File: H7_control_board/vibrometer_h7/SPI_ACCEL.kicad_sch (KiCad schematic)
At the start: 8 parts, among them J601 Conn_01x08_Socket, J602 Conn_01x08_Socket

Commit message: working on getting ERC to run... almost there!
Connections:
- net SPI_CS: no longer names the net of J602.2 (Pin_2), XL601.12 (CS)
- net SPI_MISO: no longer names the net of J602.5 (Pin_5), XL601.1 (SDO/SA0)
- net SPI_MOSI: no longer names the net of J602.4 (Pin_4), XL601.14 (SDA)
- net SPI_SCLK: no longer names the net of J602.3 (Pin_3), XL601.13 (SCL)
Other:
- note added: "SPI_CS"
- note added: "SPI_INT1"
- note added: "SPI_INT2"
- note added: "SPI_MISO"
- note added: "SPI_MOSI"
- note added: "SPI_SCLK"
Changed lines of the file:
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@@
-	)
-	(junction
-		(at 133.35 92.71)
-		(diameter 0)
-		(color 0 0 0 0)
 	)
 	(junction
@@
 	)
 	(junction
-		(at 133.35 87.63)
-		(diameter 0)
-		(color 0 0 0 0)
-	)
-	(junction
-		(at 133.35 90.17)
-		(diameter 0)
-		(color 0 0 0 0)
-	)
-	(junction
-		(at 133.35 85.09)
-		(diameter 0)
-		(color 0 0 0 0)
-	)
-	(junction
-		(at 133.35 80.01)
-		(diameter 0)
-		(color 0 0 0 0)
-	)
-	(junction
 		(at 165.1 64.77)
 		(diameter 0)
 		(color 0 0 0 0)
 	)
-	(junction
-		(at 133.35 82.55)
-		(diameter 0)
-		(color 0 0 0 0)
-	)
 	(no_connect
 		(at 149.86 82.55)
@@
 	(wire
 		(pts
-			(xy 115.57 87.63) (xy 133.35 87.63)
-		)
-		(stroke
-			(width 0)
-			(type default)
-		)
-	)
-	(wire
-		(pts
 			(xy 149.86 77.47) (xy 144.78 77.47)
 		)
@@
 	(wire
 		(pts
-			(xy 115.57 82.55) (xy 133.35 82.55)
-		)
-		(stroke
-			(width 0)
-			(type default)
-		)
-	)
-	(wire
-		(pts
-			(xy 115.57 92.71) (xy 133.35 92.71)
-		)
-		(stroke
-			(width 0)
-			(type default)
-		)
-	)
-	(wire
-		(pts
-			(xy 115.57 85.09) (xy 133.35 85.09)
-		)
-		(stroke
-			(width 0)
-			(type default)
-		)
-	)
-	(wire
-		(pts
 			(xy 133.35 90.17) (xy 149.86 90.17)
 		)
@@
 	(wire
 		(pts
-			(xy 115.57 80.01) (xy 133.35 80.01)
-		)
-		(stroke
-			(width 0)
-			(type default)
-		)
-	)
-	(wire
-		(pts
 			(xy 133.35 80.01) (xy 140.97 80.01)
 		)
@@
 		(pts
 			(xy 205.74 76.2) (xy 226.06 76.2)
-		)
-		(stroke
-			(width 0)
-			(type default)
-		)
-	)
-	(wire
-		(pts
-			(xy 115.57 90.17) (xy 133.35 90.17)
 		)
 		(stroke
@@
 		)
 	)
-	(label "SPI_INT1"
-		(at 115.57 80.01 0)
-		(fields_autoplaced yes)
-		(effects
-			(font
-				(size 1.27 1.27)
-			)
-			(justify left bottom)
+	(text "SPI_SCLK"
+		(exclude_from_sim no)
+		(at 126.746 91.186 0)
+		(effects
+			(font
+				(size 1.27 1.27)
+			)
+			(justify right bottom)
+		)
+	)
+	(text "SPI_INT2"
+		(exclude_from_sim no)
+		(at 126.746 83.566 0)
+		(effects
+			(font
+				(size 1.27 1.27)
+			)
+			(justify right bottom)
+		)
+	)
+	(text "SPI_MOSI"
+		(exclude_from_sim no)
+		(at 126.746 88.646 0)
+		(effects
+			(font
+				(size 1.27 1.27)
+			)
+			(justify right bottom)
+		)
+	)
+	(text "SPI_MISO"
+		(exclude_from_sim no)
+		(at 126.746 86.106 0)
+		(effects
+			(font
+				(size 1.27 1.27)
+			)
+			(justify right bottom)
+		)
+	)
+	(text "SPI_CS"
+		(exclude_from_sim no)
+		(at 126.746 93.726 0)
+		(effects
+			(font
+				(size 1.27 1.27)
+			)
+			(justify right bottom)
+		)
+	)
+	(text "SPI_INT1"
+		(exclude_from_sim no)
+		(at 126.746 81.026 0)
+		(effects
+			(font
+				(size 1.27 1.27)
+			)
+			(justify right bottom)
 		)
 	)
@@
 		)
 	)
-	(label "SPI_INT2"
-		(at 115.57 82.55 0)
-		(fields_autoplaced yes)
-		(effects
-			(font
-				(size 1.27 1.27)
-			)
-			(justify left bottom)
-		)
-	)
 	(label "INT1"
 		(at 140.97 80.01 180)
@@
 		)
 	)
-	(label "SPI_CS"
-		(at 115.57 92.71 0)
-		(fields_autoplaced yes)
-		(effects
-			(font
-				(size 1.27 1.27)
-			)
-			(justify left bottom)
-		)
-	)
 	(label "INT2"
 		(at 140.97 82.55 180)
@@
 		)
 	)
-	(label "SPI_MOSI"
-		(at 115.57 87.63 0)
-		(fields_autoplaced yes)
-		(effects
-			(font
-				(size 1.27 1.27)
-			)
-			(justify left bottom)
-		)
-	)
-	(label "SPI_MISO"
-		(at 115.57 85.09 0)
-		(fields_autoplaced yes)
-		(effects
-			(font
-				(size 1.27 1.27)
-			)
-			(justify left bottom)
-		)
-	)
-	(label "SPI_SCLK"
-		(at 115.57 90.17 0)
-		(fields_autoplaced yes)
-		(effects
-			(font
-				(size 1.27 1.27)
-			)
-			(justify left bottom)
-		)
-	)

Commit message: started part selection
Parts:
- C601, C602: footprint (none) -> Capacitor_SMD:C_0603_1608Metric
- XL601: LCSC (none) -> C967633
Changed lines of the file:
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@@
 			)
 		)
-		(property "Footprint" ""
+		(property "Footprint" "Capacitor_SMD:C_0603_1608Metric"
 			(at 206.7052 72.39 0)
 			(effects
@@
 			)
 		)
-		(property "Footprint" ""
+		(property "Footprint" "Capacitor_SMD:C_0603_1608Metric"
 			(at 195.2752 72.39 0)
 			(effects
@@
 			(at 165.1 85.09 0)
 			(effects
+				(font
+					(size 1.27 1.27)
+				)
+				(hide yes)
+			)
+		)
+		(property "LCSC" "C967633"
+			(at 165.1 85.09 0)
+			(effects

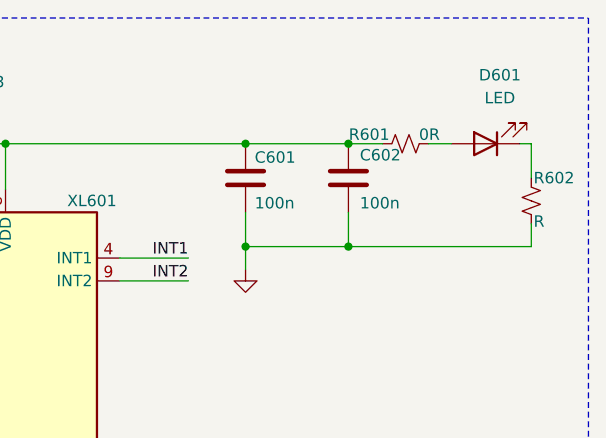
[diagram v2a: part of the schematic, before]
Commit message: component selection, headphone amp circuit specs
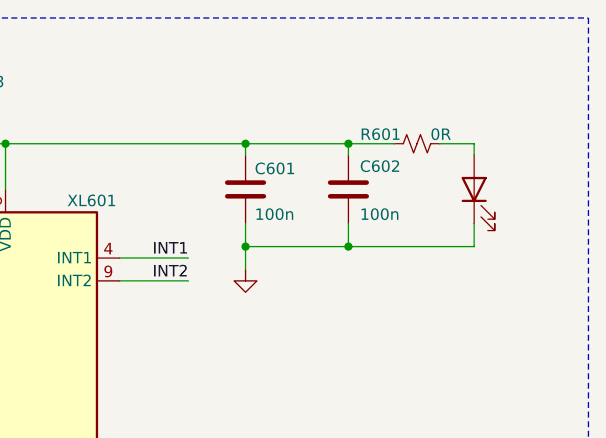
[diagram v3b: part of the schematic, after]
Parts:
- removed R602: R, symbol Device:R_Small_US
- C601, C602: footprint Capacitor_SMD:C_0603_1608Metric -> Capacitor_SMD:C_0402_1005Metric_Pad0.74x0.62mm_HandSolder; LCSC (none) -> C307331
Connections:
- net GND: now also D601.1 (K)
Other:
- moved on the sheet: C601, C602, R601
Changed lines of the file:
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@@
 	(wire
 		(pts
-			(xy 205.74 72.39) (xy 205.74 76.2)
+			(xy 205.74 73.66) (xy 205.74 76.2)
 		)
 		(stroke
@@
 	(wire
 		(pts
-			(xy 226.06 64.77) (xy 226.06 68.58)
-		)
-		(stroke
-			(width 0)
-			(type default)
-		)
-	)
-	(wire
-		(pts
 			(xy 80.01 80.01) (xy 86.36 80.01)
 		)
@@
 	(wire
 		(pts
-			(xy 214.63 64.77) (xy 217.17 64.77)
+			(xy 215.9 64.77) (xy 219.71 64.77)
 		)
 		(stroke
@@
 	(wire
 		(pts
+			(xy 194.31 66.04) (xy 194.31 64.77)
+		)
+		(stroke
+			(width 0)
+			(type default)
+		)
+	)
+	(wire
+		(pts
+			(xy 219.71 73.66) (xy 219.71 76.2)
+		)
+		(stroke
+			(width 0)
+			(type default)
+		)
+	)
+	(wire
+		(pts
 			(xy 133.35 90.17) (xy 149.86 90.17)
 		)
@@
 	(wire
 		(pts
+			(xy 205.74 66.04) (xy 205.74 64.77)
+		)
+		(stroke
+			(width 0)
+			(type default)
+		)
+	)
+	(wire
+		(pts
 			(xy 167.64 64.77) (xy 167.64 69.85)
 		)
@@
 	(wire
 		(pts
-			(xy 194.31 72.39) (xy 194.31 76.2)
+			(xy 194.31 73.66) (xy 194.31 76.2)
 		)
 		(stroke
@@
 	(wire
 		(pts
-			(xy 205.74 76.2) (xy 226.06 76.2)
-		)
-		(stroke
-			(width 0)
-			(type default)
-		)
-	)
-	(wire
-		(pts
-			(xy 226.06 73.66) (xy 226.06 76.2)
-		)
-		(stroke
-			(width 0)
-			(type default)
-		)
-	)
-	(wire
-		(pts
-			(xy 224.79 64.77) (xy 226.06 64.77)
+			(xy 205.74 76.2) (xy 219.71 76.2)
 		)
 		(stroke
@@
 	(wire
 		(pts
-			(xy 205.74 64.77) (xy 209.55 64.77)
+			(xy 205.74 64.77) (xy 210.82 64.77)
 		)
 		(stroke
@@
 		(pts
 			(xy 165.1 64.77) (xy 167.64 64.77)
+		)
+		(stroke
+			(width 0)
+			(type default)
+		)
+	)
+	(wire
+		(pts
+			(xy 219.71 64.77) (xy 219.71 66.04)
 		)
 		(stroke
@@
 	(symbol
 		(lib_id "Device:C")
-		(at 205.74 68.58 0)
+		(at 205.74 69.85 0)
 		(unit 1)
 		(exclude_from_sim no)
@@
 		(dnp no)
 		(property "Reference" "C602"
-			(at 207.01 66.04 0)
+			(at 207.01 67.31 0)
 			(effects
 				(font
@@
 		)
 		(property "Value" "100n"
-			(at 207.01 71.374 0)
+			(at 207.01 72.644 0)
 			(effects
 				(font
@@
 			)
 		)
-		(property "Footprint" "Capacitor_SMD:C_0603_1608Metric"
-			(at 206.7052 72.39 0)
-			(effects
-				(font
-					(size 1.27 1.27)
-				)
-				(hide yes)
-			)
-		)
-		(property "Datasheet" "~"
-			(at 205.74 68.58 0)
+		(property "Footprint" "Capacitor_SMD:C_0402_1005Metric_Pad0.74x0.62mm_HandSolder"
+			(at 206.7052 73.66 0)
+			(effects
+				(font
+					(size 1.27 1.27)
+				)
+				(hide yes)
+			)
+		)
+		(property "Datasheet" "https://wmsc.lcsc.com/wmsc/upload/file/pdf/v2/lcsc/2304140030_Samsung-Electro-Mechanics-CL05B104KB54PNC_C307331.pdf"
+			(at 205.74 69.85 0)
 			(effects
 				(font
@@
 		)
 		(property "Description" "Unpolarized capacitor"
-			(at 205.74 68.58 0)
+			(at 205.74 69.85 0)
+			(effects
+				(font
+					(size 1.27 1.27)
+				)
+				(hide yes)
+			)
+		)
+		(property "LCSC" "C307331"
+			(at 205.74 69.85 0)
 			(effects
 				(font
@@
 	)
 	(symbol
-		(lib_id "Device:R_Small_US")
-		(at 226.06 71.12 0)
-		(unit 1)
-		(exclude_from_sim no)
-		(in_bom yes)
-		(on_board yes)
-		(dnp no)
-		(property "Reference" "R602"
-			(at 226.314 68.58 0)
-			(effects
-				(font
-					(size 1.27 1.27)
-				)
-				(justify left)
-			)
-		)
-		(property "Value" "R"
-			(at 226.314 73.406 0)
-			(effects
-				(font
-					(size 1.27 1.27)
-				)
-				(justify left)
-			)
-		)
-		(property "Footprint" ""
-			(at 226.06 71.12 0)
-			(effects
-				(font
-					(size 1.27 1.27)
-				)
-				(hide yes)
-			)
-		)
-		(property "Datasheet" "~"
-			(at 226.06 71.12 0)
-			(effects
-				(font
-					(size 1.27 1.27)
-				)
-				(hide yes)
-			)
-		)
-		(property "Description" "Resistor, small US symbol"
-			(at 226.06 71.12 0)
-			(effects
-				(font
-					(size 1.27 1.27)
-				)
-				(hide yes)
-			)
-		)
-		(pin "1"
-		)
-		(pin "2"
-		)
-		(instances
-			(project "vibrometer_h7"
-				(path "/18de6987-156a-4b34-871e-cbbe1d261986/719d72ab-d813-461f-9482-52ce573716fd/4d0578b7-7312-4298-97a0-94006dea87de"
-					(reference "R602")
-					(unit 1)
-				)
-				(path "/18de6987-156a-4b34-871e-cbbe1d261986/719d72ab-d813-461f-9482-52ce573716fd/d33e5db2-c968-4012-a875-f240ab3119de"
-					(reference "R802")
-					(unit 1)
-				)
-				(path "/18de6987-156a-4b34-871e-cbbe1d261986/719d72ab-d813-461f-9482-52ce573716fd/e082b3de-4b18-4be4-ba81-d49e87b940c1"
-					(reference "R702")
-					(unit 1)
-				)
-			)
-		)
-	)
-	(symbol
 		(lib_id "Device:C")
-		(at 194.31 68.58 0)
+		(at 194.31 69.85 0)
 		(unit 1)
 		(exclude_from_sim no)
@@
 		(dnp no)
 		(property "Reference" "C601"
-			(at 195.326 66.294 0)
+			(at 195.326 67.564 0)
 			(effects
 				(font
@@
 		)
 		(property "Value" "100n"
-			(at 195.326 71.374 0)
+			(at 195.326 72.644 0)
 			(effects
 				(font
@@
 			)
 		)
-		(property "Footprint" "Capacitor_SMD:C_0603_1608Metric"
-			(at 195.2752 72.39 0)
-			(effects
-				(font
-					(size 1.27 1.27)
-				)
-				(hide yes)
-			)
-		)
-		(property "Datasheet" "~"
-			(at 194.31 68.58 0)
+		(property "Footprint" "Capacitor_SMD:C_0402_1005Metric_Pad0.74x0.62mm_HandSolder"
+			(at 195.2752 73.66 0)
+			(effects
+				(font
+					(size 1.27 1.27)
+				)
+				(hide yes)
+			)
+		)
+		(property "Datasheet" "https://wmsc.lcsc.com/wmsc/upload/file/pdf/v2/lcsc/2304140030_Samsung-Electro-Mechanics-CL05B104KB54PNC_C307331.pdf"
+			(at 194.31 69.85 0)
 			(effects
 				(font
@@
 		)
 		(property "Description" "Unpolarized capacitor"
-			(at 194.31 68.58 0)
+			(at 194.31 69.85 0)
+			(effects
+				(font
+					(size 1.27 1.27)
+				)
+				(hide yes)
+			)
+		)
+		(property "LCSC" "C307331"
+			(at 194.31 69.85 0)
 			(effects
 				(font
@@
 	(symbol
 		(lib_id "Device:R_Small_US")
-		(at 212.09 64.77 90)
+		(at 213.36 64.77 90)
 		(unit 1)
 		(exclude_from_sim no)
@@
 		(dnp no)
 		(property "Reference" "R601"
-			(at 210.312 63.754 90)
+			(at 211.582 63.754 90)
 			(effects
 				(font
@@
 		)
 		(property "Value" "0R"
-			(at 215.9 63.754 90)
+			(at 217.17 63.754 90)
 			(effects
 				(font
@@
 		)
 		(property "Footprint" ""
-			(at 212.09 64.77 0)
+			(at 213.36 64.77 0)
 			(effects
 				(font
@@
 		)
 		(property "Datasheet" "~"
-			(at 212.09 64.77 0)
+			(at 213.36 64.77 0)
 			(effects
 				(font
@@
 		)
 		(property "Description" "Resistor, small US symbol"
-			(at 212.09 64.77 0)
+			(at 213.36 64.77 0)
 			(effects
 				(font
@@
 	(symbol
 		(lib_id "Device:LED")
-		(at 220.98 64.77 180)
+		(at 219.71 69.85 90)
 		(unit 1)
 		(exclude_from_sim no)
@@
 		(fields_autoplaced yes)
 		(property "Reference" "D601"
-			(at 222.5675 57.15 0)
-			(effects
-				(font
-					(size 1.27 1.27)
-				)
+			(at 223.52 70.1674 90)
+			(effects
+				(font
+					(size 1.27 1.27)
+				)
+				(justify right)
+				(hide yes)
 			)
 		)
 		(property "Value" "LED"
-			(at 222.5675 59.69 0)
-			(effects
-				(font
-					(size 1.27 1.27)
-				)
+			(at 223.52 72.7074 90)
+			(effects
+				(font
+					(size 1.27 1.27)
+				)
+				(justify right)
+				(hide yes)
 			)
 		)
 		(property "Footprint" ""
-			(at 220.98 64.77 0)
+			(at 219.71 69.85 0)
 			(effects
 				(font
@@
 		)
 		(property "Datasheet" "~"
-			(at 220.98 64.77 0)
+			(at 219.71 69.85 0)
 			(effects
 				(font
@@
 		)
 		(property "Description" "Light emitting diode"
-			(at 220.98 64.77 0)
-			(effects
-				(font
+			(at 219.71 69.85 0)
+			(effects
+				(font

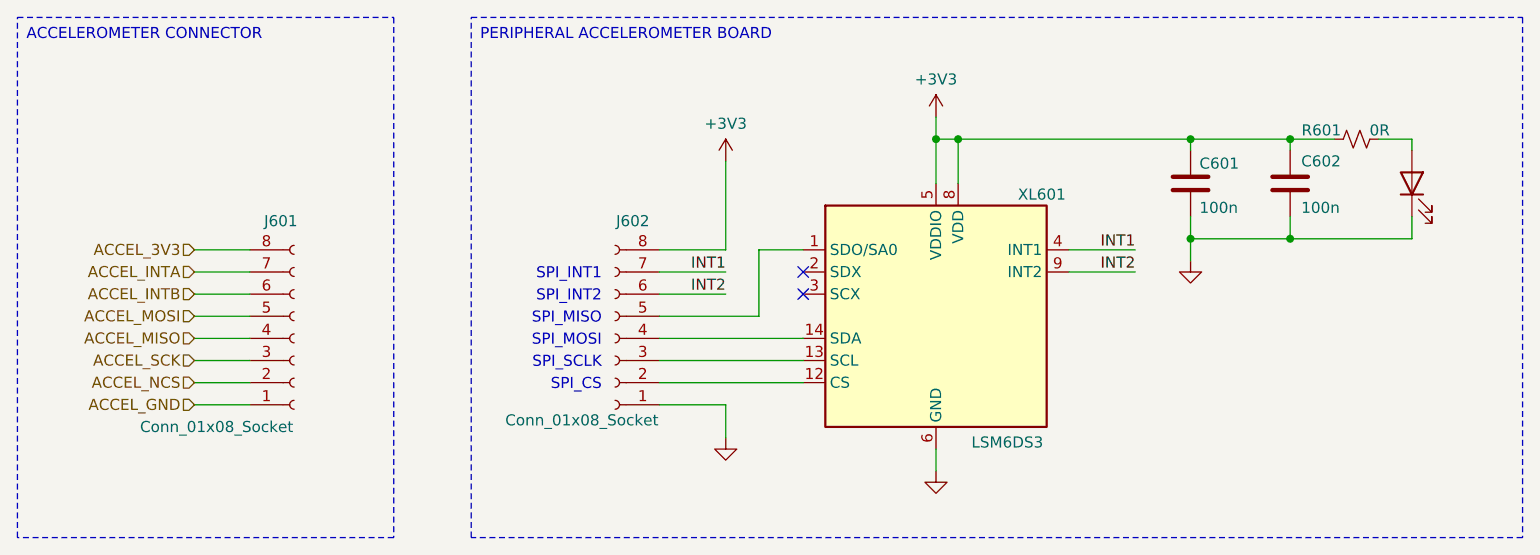
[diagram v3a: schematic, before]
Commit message: part selection for audio, schematic cleanup
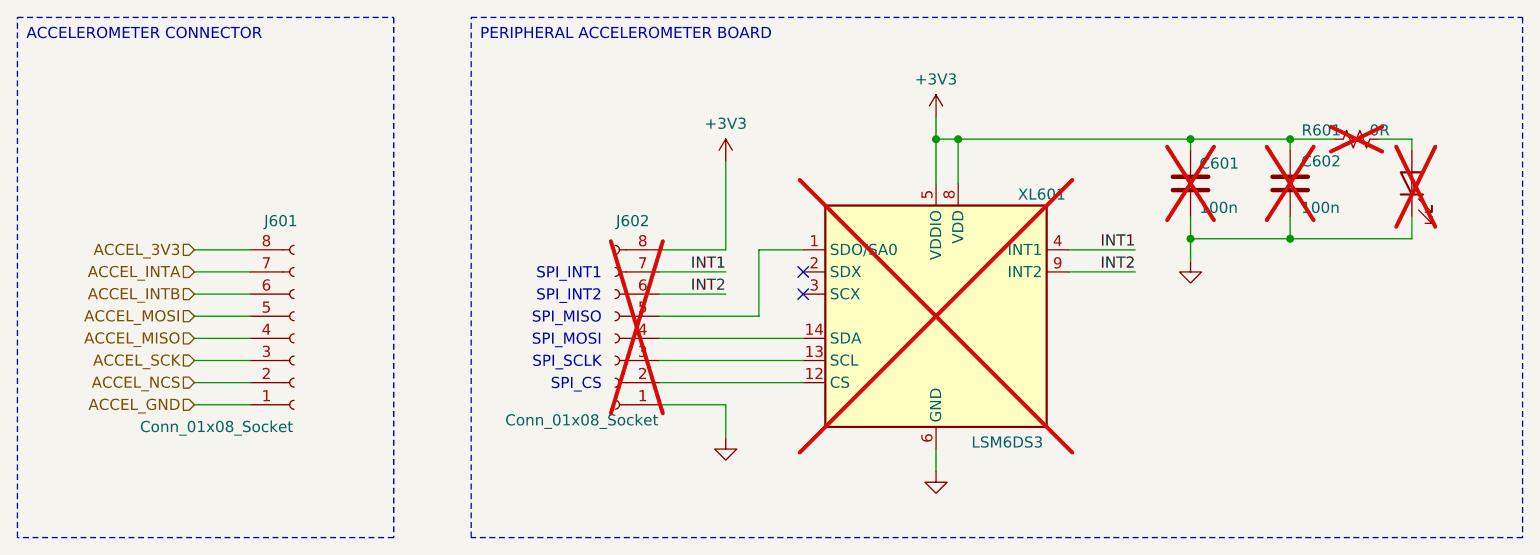
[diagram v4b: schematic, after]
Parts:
- C601, C602, D601, J602, R601, XL601: now not fitted
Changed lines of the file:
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@@
 		(in_bom yes)
 		(on_board yes)
-		(dnp no)
+		(dnp yes)
 		(property "Reference" "C602"
 			(at 207.01 67.31 0)
@@
 		(in_bom yes)
 		(on_board yes)
-		(dnp no)
+		(dnp yes)
 		(property "Reference" "C601"
 			(at 195.326 67.564 0)
@@
 		(in_bom yes)
 		(on_board yes)
-		(dnp no)
+		(dnp yes)
 		(property "Reference" "XL601"
 			(at 174.498 71.12 0)
@@
 		(in_bom yes)
 		(on_board yes)
-		(dnp no)
+		(dnp yes)
 		(property "Reference" "R601"
 			(at 211.582 63.754 90)
@@
 		(in_bom yes)
 		(on_board yes)
-		(dnp no)
+		(dnp yes)
 		(property "Reference" "J602"
 			(at 130.302 74.168 0)
@@
 		(in_bom yes)
 		(on_board yes)
-		(dnp no)
+		(dnp yes)
 		(fields_autoplaced yes)
 		(property "Reference" "D601"

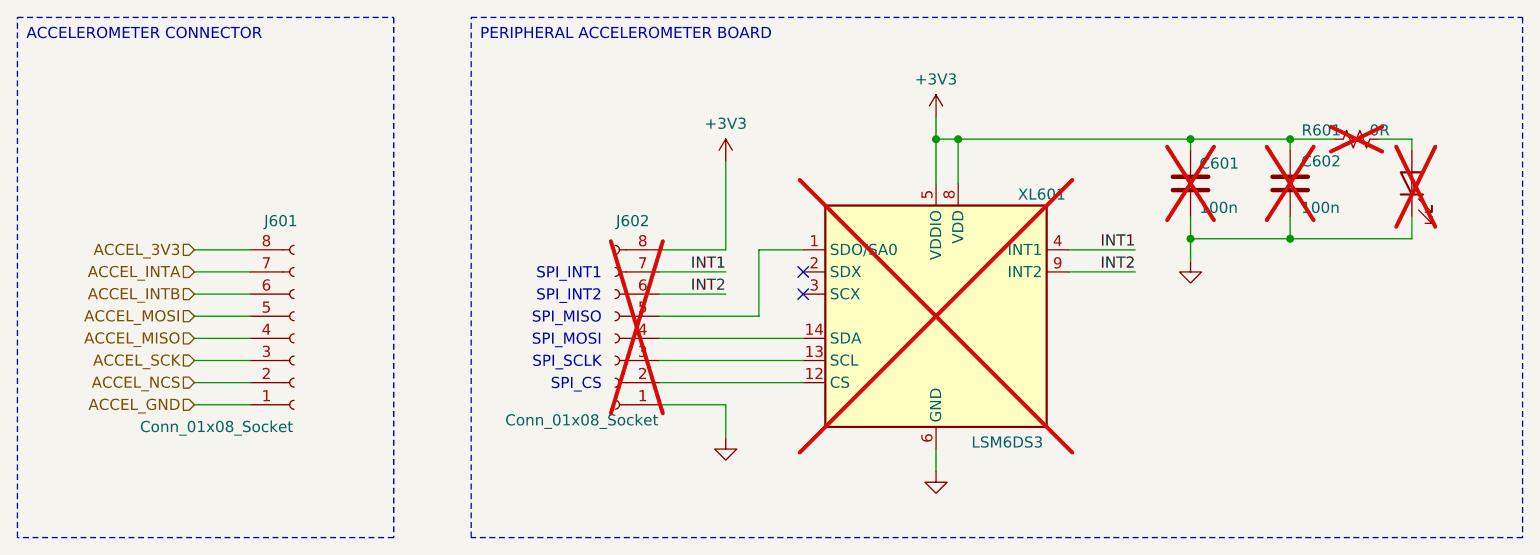
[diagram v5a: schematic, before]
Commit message: selected strobe LEDs, schematic cleanup
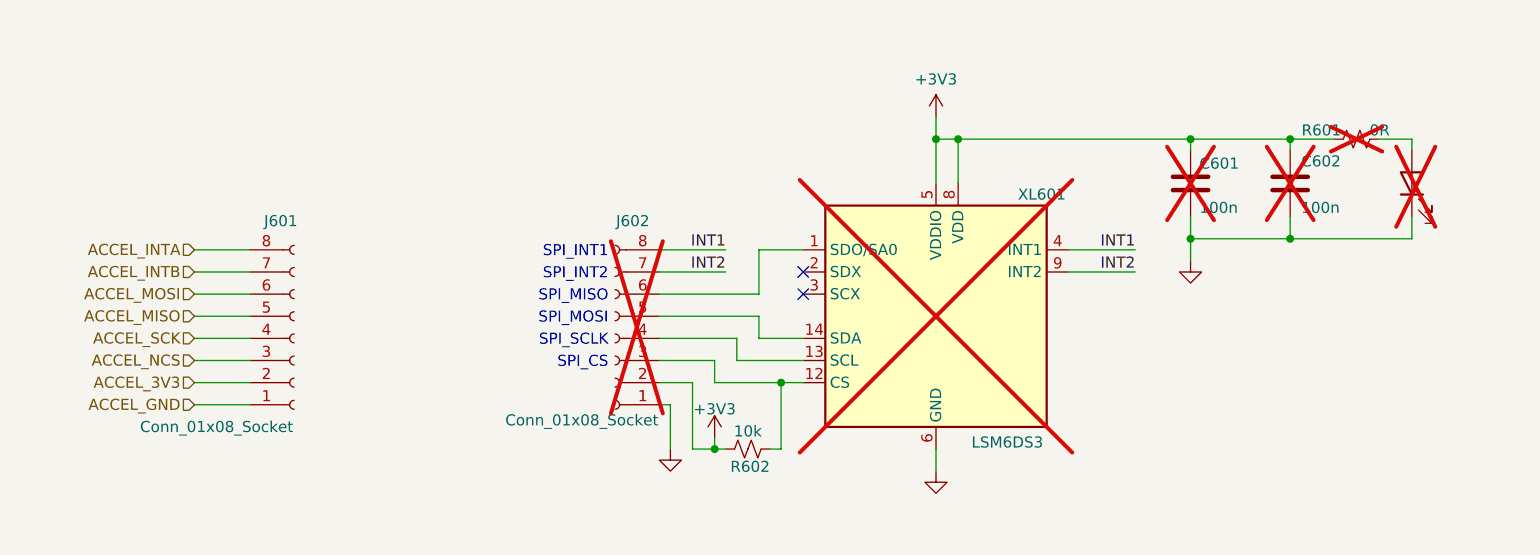
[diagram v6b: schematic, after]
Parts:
- added R602: 10k, symbol Device:R_Small_US
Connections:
- net +3V3: now also J602.2 (Pin_2), R602.2; no longer J602.8 (Pin_8)
- net ACCEL_3V3: now also J601.2 (Pin_2); no longer J601.8 (Pin_8)
- net ACCEL_INTA: now also J601.8 (Pin_8); no longer J601.7 (Pin_7)
- net ACCEL_INTB: now also J601.7 (Pin_7); no longer J601.6 (Pin_6)
- net ACCEL_MISO: now also J601.5 (Pin_5); no longer J601.4 (Pin_4)
- net ACCEL_MOSI: now also J601.6 (Pin_6); no longer J601.5 (Pin_5)
- net ACCEL_NCS: now also J601.3 (Pin_3); no longer J601.2 (Pin_2)
- net ACCEL_SCK: now also J601.4 (Pin_4); no longer J601.3 (Pin_3)
- net INT1: now also J602.8 (Pin_8); no longer J602.7 (Pin_7)
- net INT2: now also J602.7 (Pin_7); no longer J602.6 (Pin_6)
- net at XL601.1 (SDO/SA0): now also J602.6 (Pin_6); no longer J602.5 (Pin_5)
- net at XL601.12 (CS): now also J602.3 (Pin_3), R602.1; no longer J602.2 (Pin_2)
- net at XL601.13 (SCL): now also J602.4 (Pin_4); no longer J602.3 (Pin_3)
- net at XL601.14 (SDA): now also J602.5 (Pin_5); no longer J602.4 (Pin_4)
